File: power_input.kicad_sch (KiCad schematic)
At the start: 99 parts, among them J201 61300211121, J202 61300211121, J203 61300211121, J204 61300211121, J205 61300211121, J206 61300211121, J207 61300211121, J208 61300211121, Q201 SQ2319CES, Q202 IRFL4315TRPBF, Q203 SQ2319CES, Q204 IRFL4315TRPBF, Q205 SQ2319CES, Q206 SQ2319CES, U201 LM397, U202 OPA197, U203 LM397, U204 LM397

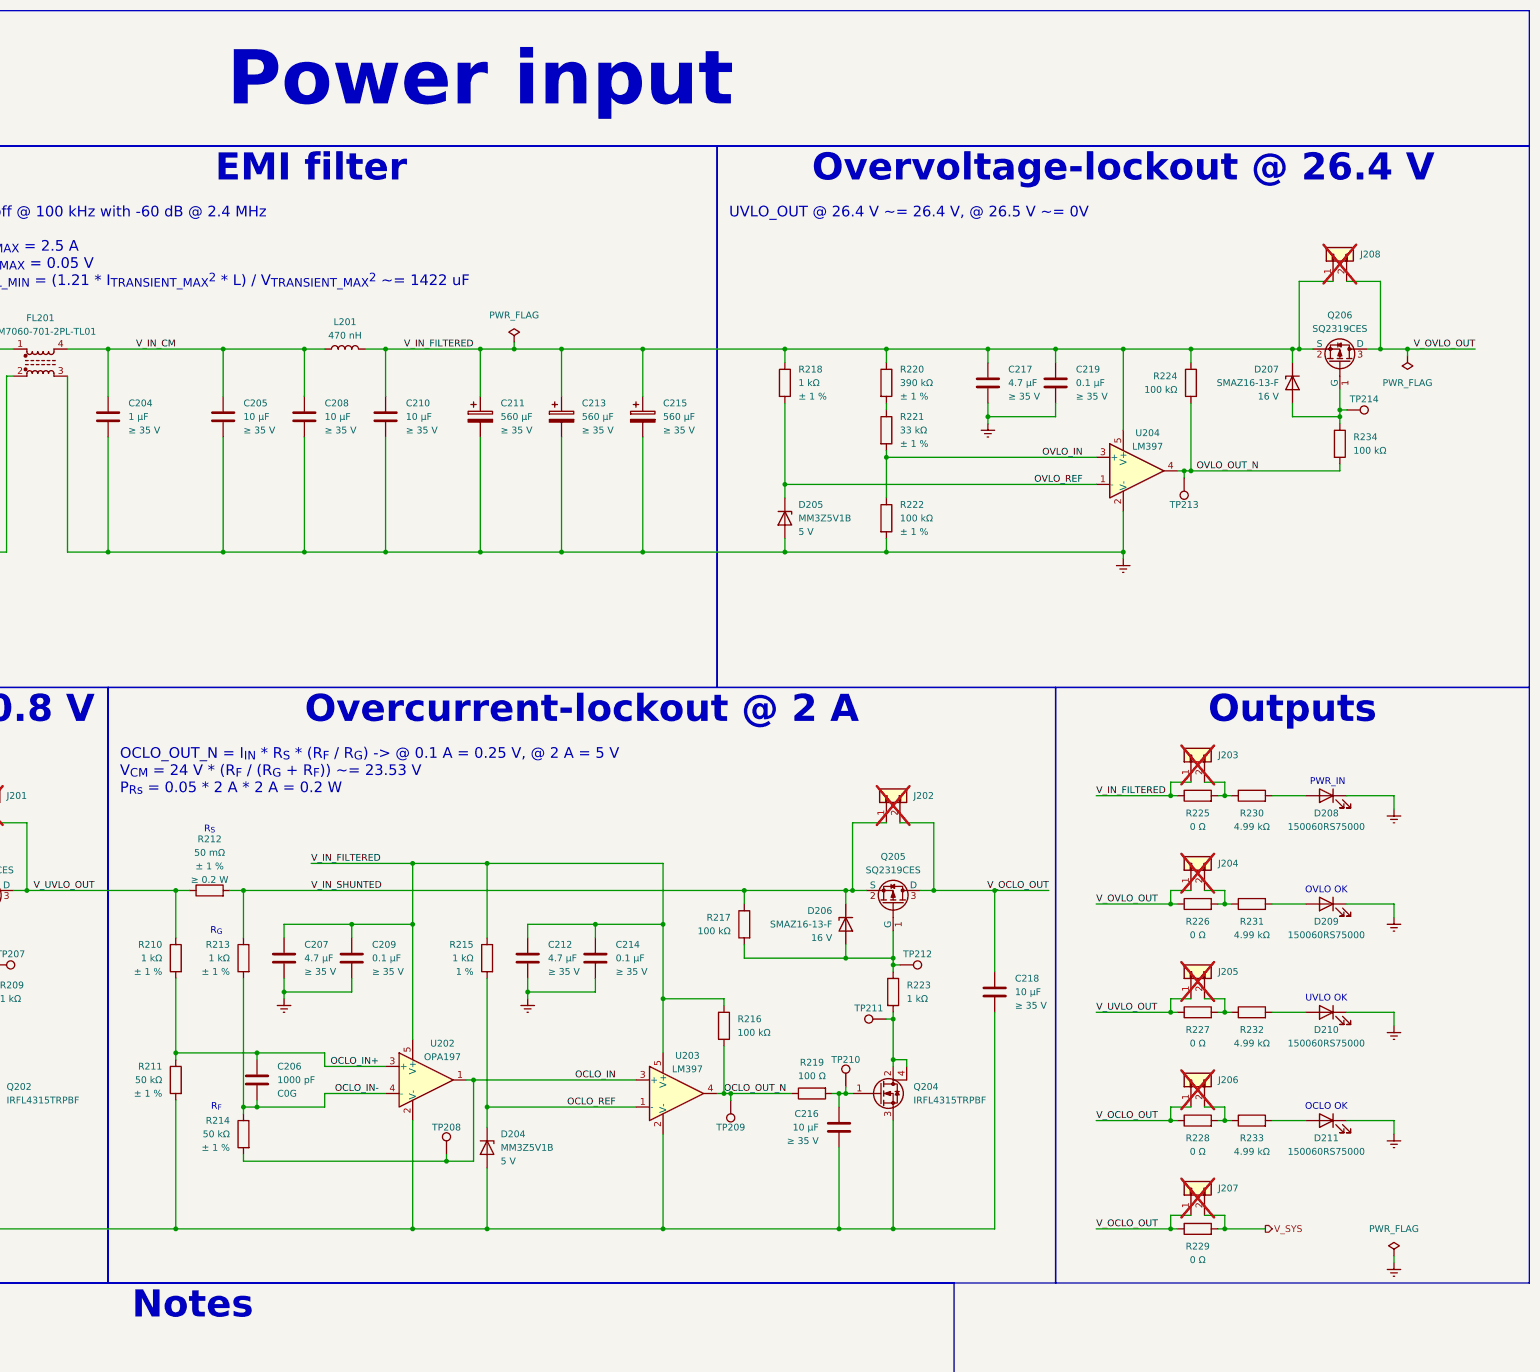
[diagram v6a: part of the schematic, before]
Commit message: Add MPU power generation
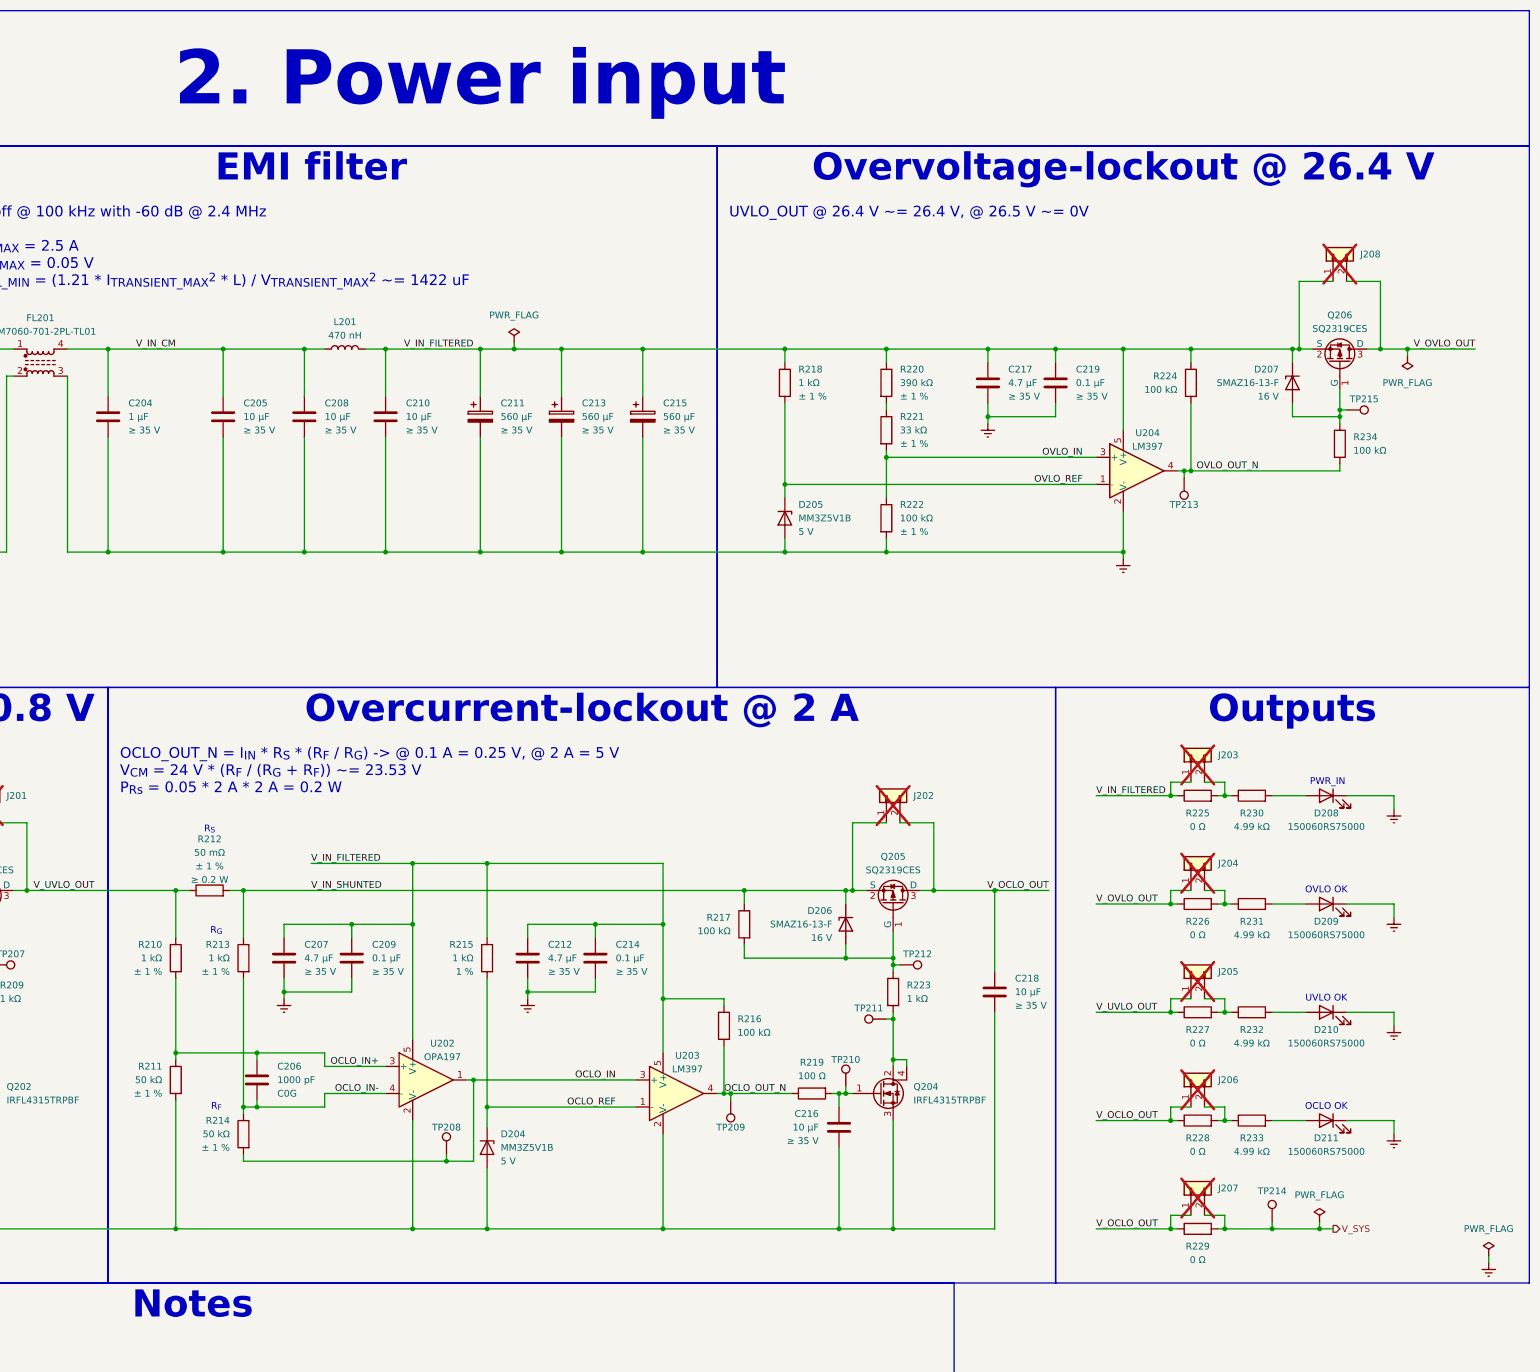
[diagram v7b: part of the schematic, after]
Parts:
- added TP214: TestPoint, TestPoint:TestPoint_Pad_D1.0mm, symbol Connector:TestPoint
- renumbered TP214 to TP215
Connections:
- net V_SYS: now also TP214.1

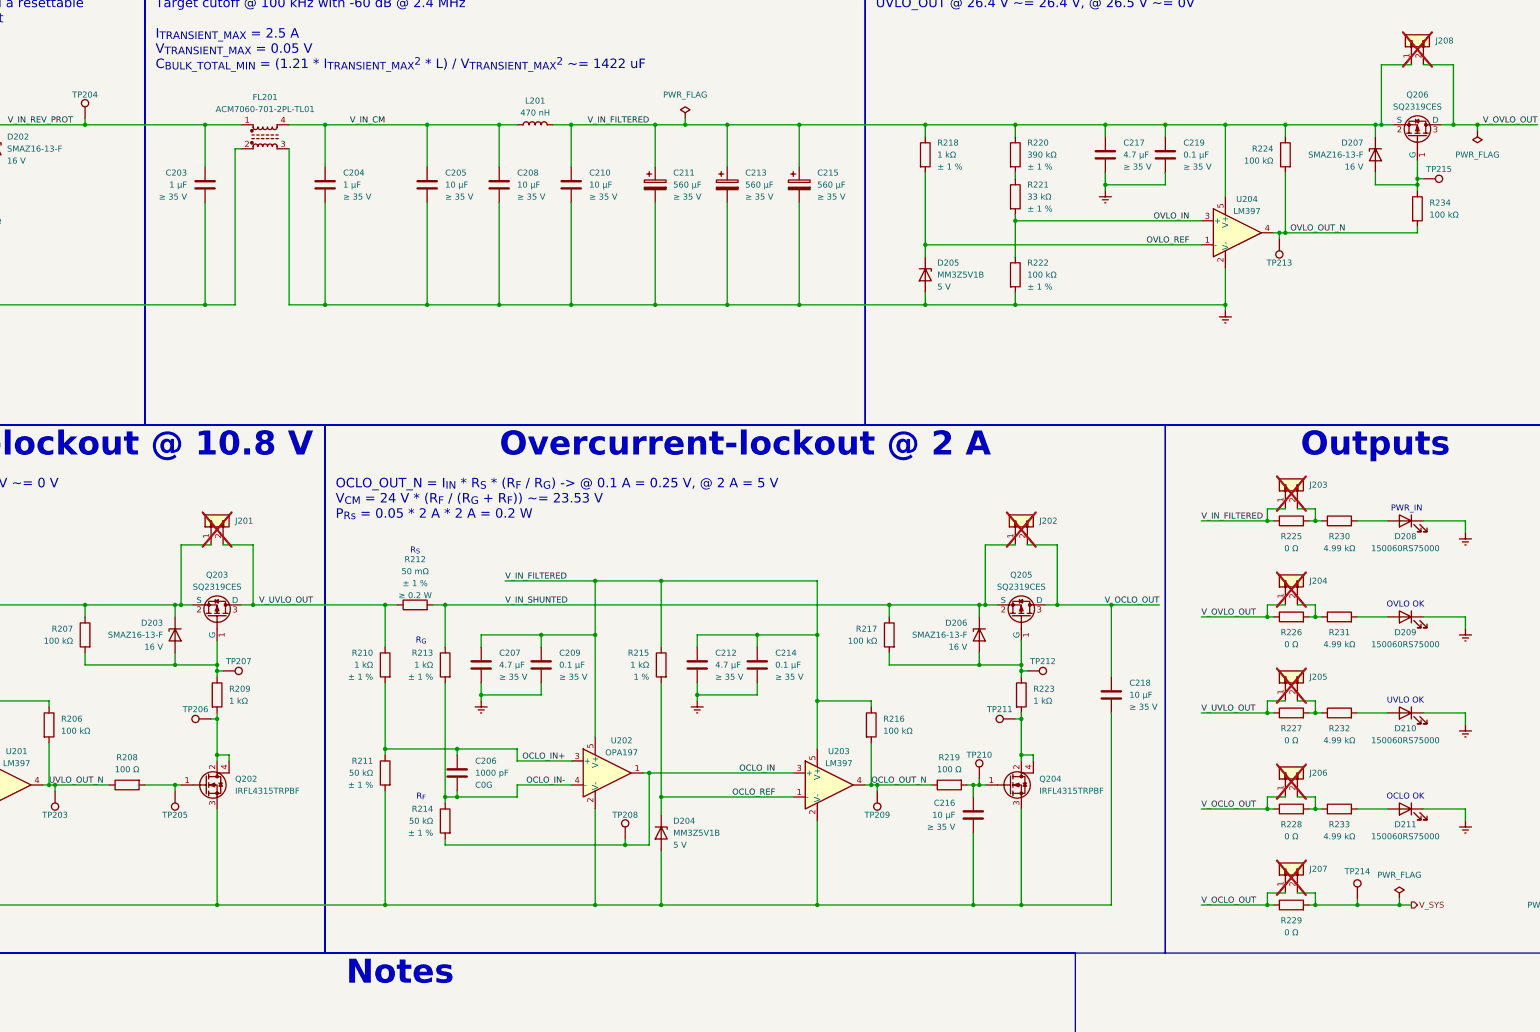
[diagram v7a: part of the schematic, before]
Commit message: Add test points, assign netclasses and clean-up
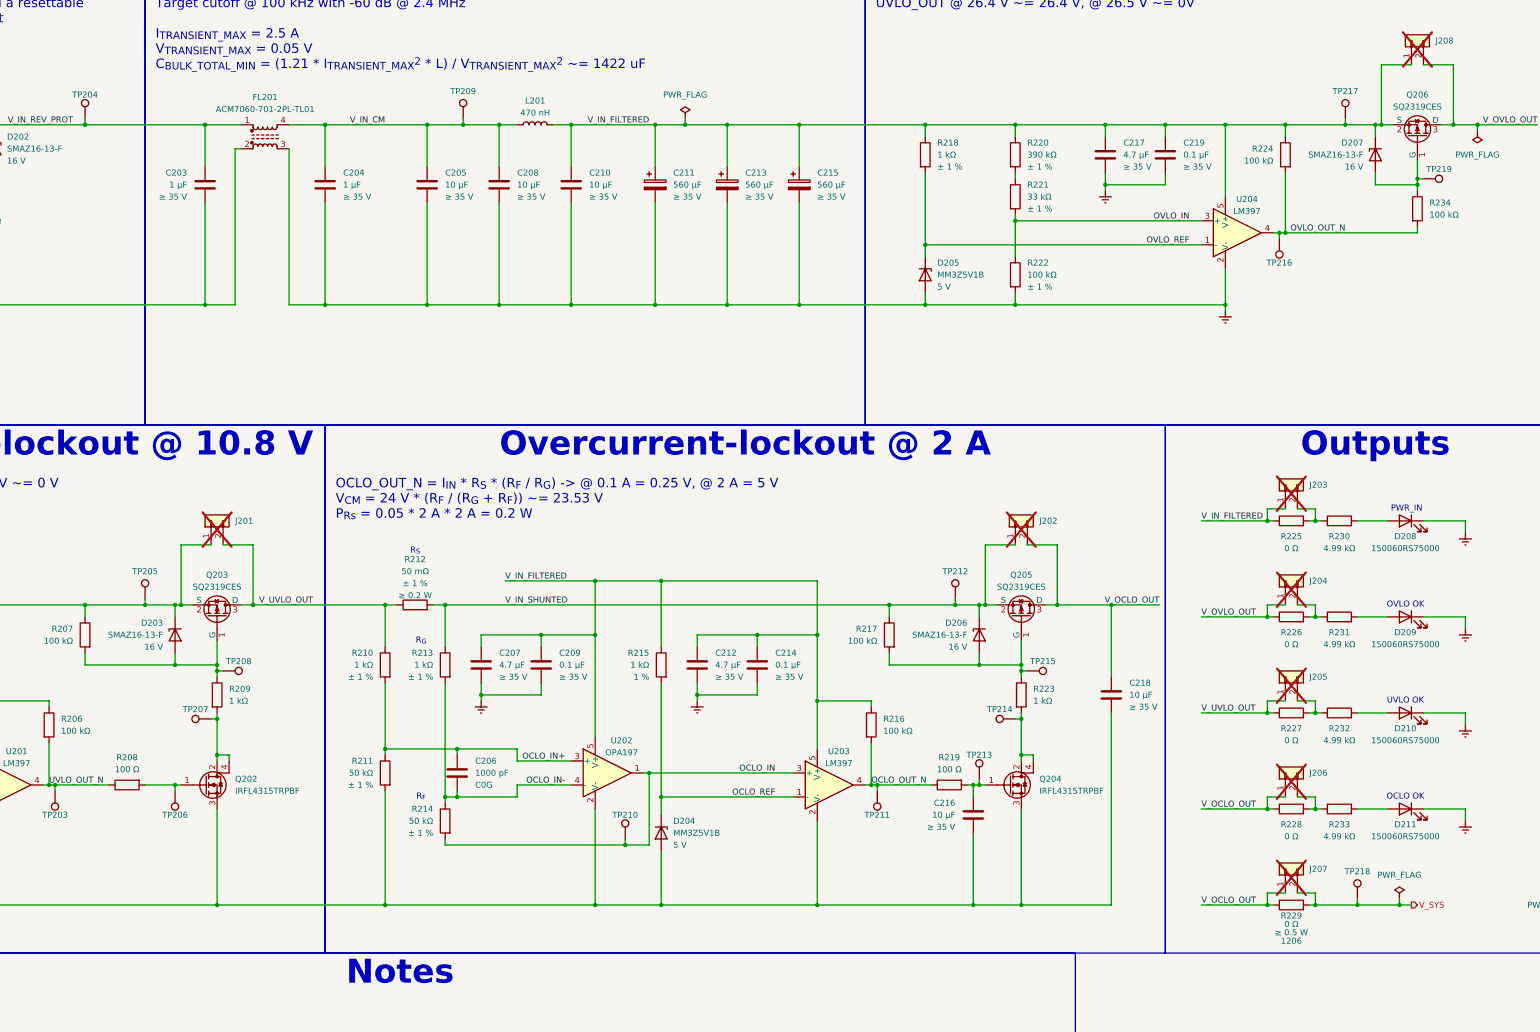
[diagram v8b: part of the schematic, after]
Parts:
- added TP205, TP209, TP212, TP217: TestPoint, TestPoint:TestPoint_Pad_D1.0mm, symbol Connector:TestPoint
- R229: footprint Resistor_SMD:R_0805_2012Metric -> (none); DigiKey Part Number 732-560112120002CT-ND -> (none); MPN 560112120002 -> (none); Manufacturer Würth Elektronik -> (none); Power (none) -> ≥ 0.5 W; Size (none) -> 1206
- renumbered TP205 to TP206, TP206 to TP207, TP207 to TP208, TP208 to TP210, TP209 to TP211, TP210 to TP213, TP211 to TP214, TP212 to TP215, TP213 to TP216, TP214 to TP218, TP215 to TP219
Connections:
- net V_IN_CM: now also TP209.1
- net V_IN_FILTERED: now also TP217.1
- net V_IN_SHUNTED: now also TP212.1
- net V_OVLO_OUT: now also TP205.1
